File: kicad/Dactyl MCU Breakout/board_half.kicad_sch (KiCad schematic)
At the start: 18 parts, among them J3 Columns, J4 Thumbs, J5 Rows, J6 Extrernal, J7 Split, J8 JST, SW1 LED, SW2 Reset, SW3 Battery, U1 Nice!Nano/2040

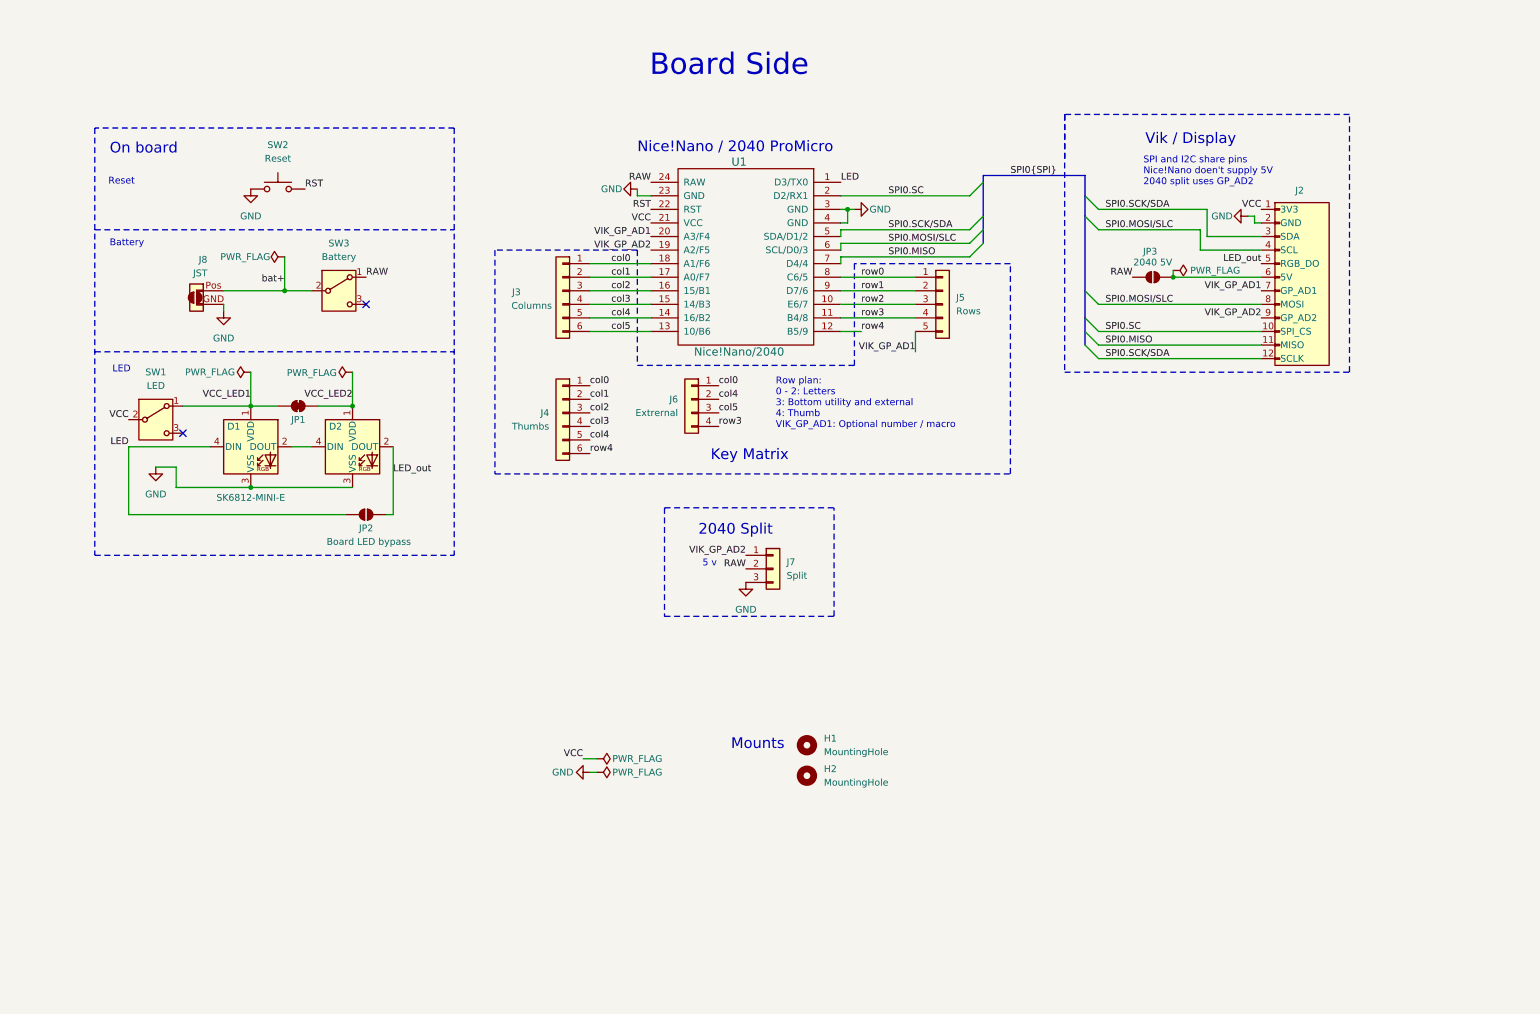
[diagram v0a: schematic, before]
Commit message: feat: add column to thumb, shift split to Vik AD1
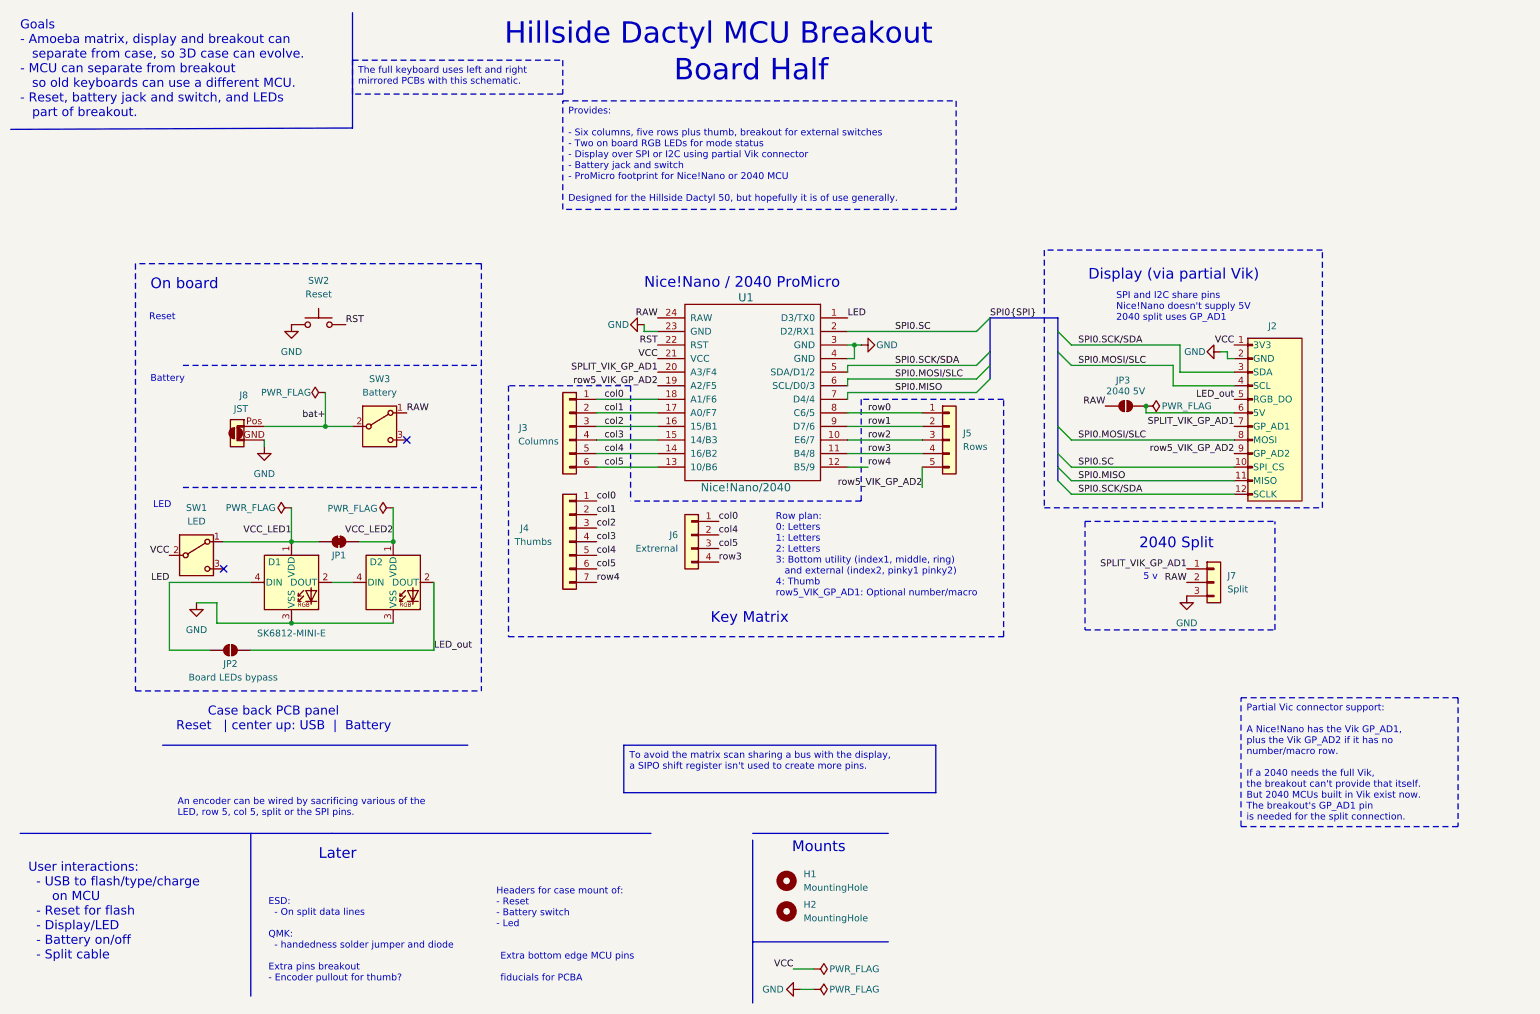
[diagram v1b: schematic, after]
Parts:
- removed J4: Thumbs, Connector_PinHeader_2.54mm:PinHeader_1x06_P2.54mm_Vertical, symbol Connector_Generic:Conn_01x06
- added J4: Thumbs, symbol Connector_Generic:Conn_01x07
- JP2: value Board LED bypass -> Board LEDs bypass
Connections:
- net col0: now also J4.1 (Pin_1)
- net col1: now also J4.2 (Pin_2)
- net col2: now also J4.3 (Pin_3)
- net col3: now also J4.4 (Pin_4)
- net col4: now also J4.5 (Pin_5)
- net col5: now also J4.6 (Pin_6)
- net row4: now also J4.7 (Pin_7)
- net VIK_GP_AD1 renamed SPLIT_VIK_GP_AD1
- net SPLIT_VIK_GP_AD1: now also J7.1 (Pin_1); no longer J5.5 (Pin_5)
- net VIK_GP_AD2 renamed row5_VIK_GP_AD2
- net row5_VIK_GP_AD2: now also J5.5 (Pin_5); no longer J7.1 (Pin_1)
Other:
- note added: "${TITLE}"
- note added: "An encoder can be wired by sacrificing various of the LED, row 5, col 5, split or the SPI pins."
- note added: "Board Half"
- note added: "Case back PCB panel Reset | center up: USB | Battery"
- note added: "Display (via partial Vik)"
- note added: "ESD: - On split data lines QMK: - handedness solder jumper and diode Extra pins breakout - Encoder pullout for thumb?"
- note added: "Extra bottom edge MCU pins fiducials for PCBA"
- note added: "Goals - Amoeba matrix, display and breakout can separate from case, so 3D case can evolve. - MCU can separate from breakout so old keyboards can use a different MCU. - Reset, battery jack and switch, and LEDs part of breakout."
- note added: "Headers for case mount of: - Reset - Battery switch - Led"
- note added: "Later"
- note added: "Row plan: 0: Letters 1: Letters 2: Letters 3: Bottom utility (index1, middle, ring) and external (index2, pinky1 pinky2) 4: Thumb row5_VIK_GP_AD1: Optional number/macro"
- note added: "SPI and I2C share pins Nice!Nano doesn't supply 5V 2040 split uses GP_AD1"
- note added: "User interactions: - USB to flash/type/charge on MCU - Reset for flash - Display/LED - Battery on/off - Split cable"
- note removed: "Board Side"
- note removed: "Row plan: 0 - 2: Letters 3: Bottom utility and external 4: Thumb VIK_GP_AD1: Optional number / macro"
- note removed: "SPI and I2C share pins Nice!Nano doen't supply 5V 2040 split uses GP_AD2"
- note removed: "Vik / Display"
- title: (none) -> Hillside Dactyl MCU Breakout
- moved on the sheet: D1, D2, H1, H2, J2, J3, J5, J6, J7, J8, JP1, JP2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

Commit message: feat: finish wiring
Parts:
- removed JP3: 2040 5V, Jumper:SolderJumper-2_P1.3mm_Bridged_RoundedPad1.0x1.5mm, symbol Jumper:SolderJumper_2_Open
- added J5: Display, Connector_PinHeader_2.54mm:PinHeader_1x05_P2.54mm_Vertical, symbol Connector_Generic:Conn_01x05
- added JP3: SCK term, Jumper:SolderJumper-2_P1.3mm_Bridged_RoundedPad1.0x1.5mm, symbol Jumper:SolderJumper_2_Bridged
- D1, D2: footprint Dactyl:SK6812-MINI-E-Dog2 -> Dactyl:SK6812-MINI-E-Dog2_1S
- H1, H2: footprint MountingHole:MountingHole_3.2mm_M3_DIN965_Pad -> MountingHole:MountingHole_3.2mm_M3_DIN965
- J3: renamed from J4; footprint (none) -> Connector_PinHeader_2.54mm:PinHeader_1x07_P2.54mm_Vertical
- J6: value Extrernal -> External
- J9: renamed from J2; value ~ -> Vic; footprint (none) -> Dactyl:vik-keyboard-connector-horizontal; LCSC Part # (none) -> C2906115
- JP2: value Board LEDs bypass -> LEDs bypass
- SW1: renamed from SW3; LCSC Part # (none) -> C221662
- SW4: renamed from SW1; LCSC Part # (none) -> C221662
- U1: footprint Dactyl:ProMicro_unrouted -> Dactyl:ProMicro_v2_1
- renumbered J3 to J1, J5 to J2, J8 to J7, J7 to J8
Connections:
- net GND: now also J7.1 (GND), J5.4 (Pin_4); no longer J7.GND
- net LED: now also U1.10 (E6/7); no longer U1.1 (D3/TX0)
- net RAW: now also J9.6 (5V)
- net SPI0.SC: now also J5.5 (Pin_5)
- net SPI0.SCK/SDA: now also J5.2 (Pin_2), JP3.2 (B); no longer U1.5 (SDA/D1/2)
- net VCC: now also J5.3 (Pin_3)
- net bat+: now also J7.2 (Pos); no longer J7.Pos
- net row0: now also U1.1 (D3/TX0); no longer U1.8 (C6/5)
- net row1: now also U1.8 (C6/5); no longer U1.9 (D7/6)
- net row2: now also U1.9 (D7/6); no longer U1.10 (E6/7)
- net SPI0.MISO renamed SPI0.CIPO
- net SPI0.MOSI/SLC renamed SPI0.COPI/SCL
- net SPI0.COPI/SCL: now also J5.1 (Pin_1)
- new net: JP3.1 (A), U1.5 (SDA/D1/2)
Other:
- note added: "Display and partial Vik"
- note added: "ESD: - On split data lines QMK: - handedness solder jumper and diode Extra pins breakout - Encoder pullout for thumb? Jumper on ViK 5v to cut off Nice!Nano 3.3v?"
- note removed: "Display (via partial Vik)"
- note removed: "ESD: - On split data lines QMK: - handedness solder jumper and diode Extra pins breakout - Encoder pullout for thumb?"
- moved on the sheet: J1, J2, J3, J6, J8, J9, U1

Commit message: feat: area reserved for TRRS. base plate notch
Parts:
- JP2: value LEDs bypass -> Vik LED bypass; footprint Jumper:SolderJumper-2_P1.3mm_Bridged_RoundedPad1.0x1.5mm -> Jumper:SolderJumper-2_P1.3mm_Open_RoundedPad1.0x1.5mm
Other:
- moved on the sheet: J2, J8
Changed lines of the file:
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@@
 	(wire
 		(pts
-			(xy 173.99 93.98) (xy 168.91 93.98)
+			(xy 176.53 93.98) (xy 168.91 93.98)
 		)
 		(stroke
@@
 		)
 	)
-	(wire
-		(pts
-			(xy 190.5 93.98) (xy 190.5 97.79)
-		)
-		(stroke
-			(width 0)
-			(type default)
-		)
-	)
 	(polyline
 		(pts
-			(xy 172.72 100.33) (xy 128.27 100.33)
+			(xy 173.99 100.33) (xy 128.27 100.33)
 		)
 		(stroke
@@
 	(polyline
 		(pts
-			(xy 172.72 81.28) (xy 172.72 100.33)
+			(xy 173.99 81.28) (xy 173.99 100.33)
 		)
 		(stroke
@@
 	(wire
 		(pts
-			(xy 168.91 91.44) (xy 190.5 91.44)
+			(xy 168.91 91.44) (xy 191.77 91.44)
 		)
 		(stroke
@@
 	(polyline
 		(pts
-			(xy 198.12 148.59) (xy 198.12 128.27)
+			(xy 171.45 148.59) (xy 171.45 128.27)
 		)
 		(stroke
@@
 	(polyline
 		(pts
-			(xy 204.47 81.28) (xy 172.72 81.28)
+			(xy 204.47 81.28) (xy 173.99 81.28)
 		)
 		(stroke
@@
 	(polyline
 		(pts
-			(xy 162.56 128.27) (xy 162.56 148.59)
+			(xy 135.89 128.27) (xy 135.89 148.59)
 		)
 		(stroke
@@
 	(wire
 		(pts
-			(xy 180.34 86.36) (xy 190.5 86.36)
+			(xy 180.34 86.36) (xy 191.77 86.36)
 		)
 		(stroke
@@
 	(wire
 		(pts
-			(xy 177.8 88.9) (xy 190.5 88.9)
+			(xy 177.8 88.9) (xy 191.77 88.9)
 		)
 		(stroke
@@
 	(polyline
 		(pts
-			(xy 97.79 149.86) (xy 40.64 149.86)
+			(xy 97.79 54.61) (xy 40.64 54.61)
 		)
 		(stroke
@@
 	(wire
 		(pts
+			(xy 191.77 93.98) (xy 191.77 97.79)
+		)
+		(stroke
+			(width 0)
+			(type default)
+		)
+	)
+	(wire
+		(pts
 			(xy 50.8 127) (xy 64.77 127)
 		)
@@
 	(wire
 		(pts
+			(xy 191.77 83.82) (xy 190.5 83.82)
+		)
+		(stroke
+			(width 0)
+			(type default)
+		)
+	)
+	(wire
+		(pts
 			(xy 251.46 76.2) (xy 252.73 76.2)
 		)
@@
 	(polyline
 		(pts
-			(xy 162.56 128.27) (xy 198.12 128.27)
+			(xy 135.89 128.27) (xy 171.45 128.27)
 		)
 		(stroke
@@
 	(polyline
 		(pts
-			(xy 162.56 148.59) (xy 198.12 148.59)
+			(xy 135.89 148.59) (xy 171.45 148.59)
 		)
 		(stroke
@@
 		)
 	)
-	(text_box "Partial Vic connector support:\n\nA Nice!Nano has the Vik GP_AD1, plus the Vik GP_AD2 if it has no number/macro row.\n\nIf a 2040 needs the full Vik, the breakout can't provide that itself.\nBut 2040 MCUs built in Vik exist now."
+	(text_box "Partial Vic connector support:\n\nA Nice!Nano has the Vik GP_AD1, plus the Vik GP_AD2 \nif it has no number/macro row.\n\nIf a 2040 needs the full Vik, the breakout can't provide it.\nBut 2040 MCUs with built in Vik now exist."
 		(exclude_from_sim no)
-		(at 213.36 149.86 0)
-		(size 69.85 15.24)
+		(at 219.71 127 0)
+		(size 60.96 15.24)
 		(stroke
 			(width 0)
@@
 	(text "        Case back PCB panel\nReset   | center up: USB  |  Battery\n"
 		(exclude_from_sim no)
-		(at 43.18 147.32 0)
+		(at 43.18 52.07 0)
 		(effects
 			(font
@@
 	(text "2040 Split"
 		(exclude_from_sim no)
-		(at 172.72 133.604 0)
+		(at 146.05 133.604 0)
 		(effects
 			(font
@@
 	(text "5 v \n"
 		(exclude_from_sim no)
-		(at 173.482 139.446 0)
+		(at 146.812 139.446 0)
 		(effects
 			(font
@@
 	)
 	(label "row5_VIK_GP_AD2"
-		(at 190.5 97.79 180)
+		(at 191.77 97.79 180)
 		(fields_autoplaced yes)
 		(effects
@@
 	)
 	(label "SPLIT_VIK_GP_AD1"
-		(at 181.61 137.16 180)
+		(at 154.94 137.16 180)
 		(fields_autoplaced yes)
 		(effects
@@
 	)
 	(label "row4"
-		(at 173.99 93.98 0)
+		(at 176.53 93.98 0)
 		(fields_autoplaced yes)
 		(effects
@@
 	)
 	(label "RAW"
-		(at 181.61 139.7 180)
+		(at 154.94 139.7 180)
 		(fields_autoplaced yes)
 		(effects
@@
 			)
 		)
-		(property "Value" "LEDs bypass"
+		(property "Value" "Vik LED bypass"
 			(at 53.848 137.16 0)
 			(effects
@@
 			)
 		)
-		(property "Footprint" "Jumper:SolderJumper-2_P1.3mm_Bridged_RoundedPad1.0x1.5mm"
+		(property "Footprint" "Jumper:SolderJumper-2_P1.3mm_Open_RoundedPad1.0x1.5mm"
 			(at 53.34 132.08 0)
 			(effects
@@
 	(symbol
 		(lib_id "Connector_Generic:Conn_01x05")
-		(at 195.58 88.9 0)
+		(at 196.85 88.9 0)
 		(unit 1)
 		(exclude_from_sim no)
@@
 		(dnp no)
 		(property "Reference" "J2"
-			(at 198.12 87.6299 0)
+			(at 199.39 87.6299 0)
 			(effects
 				(font
@@
 		)
 		(property "Value" "Rows"
-			(at 198.12 90.1699 0)
+			(at 199.39 90.1699 0)
 			(effects
 				(font
@@
 		)
 		(property "Footprint" "Connector_PinHeader_2.54mm:PinHeader_1x05_P2.54mm_Vertical"
-			(at 195.58 88.9 0)
+			(at 196.85 88.9 0)
 			(effects
 				(font
@@
 		)
 		(property "Datasheet" "~"
-			(at 195.58 88.9 0)
+			(at 196.85 88.9 0)
 			(effects
 				(font
@@
 		)
 		(property "Description" "Generic connector, single row, 01x05, script generated (kicad-library-utils/schlib/autogen/connector/)"
-			(at 195.58 88.9 0)
+			(at 196.85 88.9 0)
 			(effects
 				(font
@@
 	(symbol
 		(lib_id "Connector_Generic:Conn_01x03")
-		(at 186.69 139.7 0)
+		(at 160.02 139.7 0)
 		(unit 1)
 		(exclude_from_sim no)
@@
 		(fields_autoplaced yes)
 		(property "Reference" "J8"
-			(at 189.23 138.4299 0)
+			(at 162.56 138.4299 0)
 			(effects
 				(font
@@
 		)
 		(property "Value" "Split"
-			(at 189.23 140.9699 0)
+			(at 162.56 140.9699 0)
 			(effects
 				(font
@@
 		)
 		(property "Footprint" "Connector_PinHeader_2.54mm:PinHeader_1x03_P2.54mm_Vertical"
-			(at 186.69 139.7 0)
+			(at 160.02 139.7 0)
 			(effects
 				(font
@@
 		)
 		(property "Datasheet" "~"
-			(at 186.69 139.7 0)
+			(at 160.02 139.7 0)
 			(effects
 				(font
@@
 		)
 		(property "Description" ""
-			(at 186.69 139.7 0)
+			(at 160.02 139.7 0)
 			(effects
 				(font
@@
 	(symbol
 		(lib_id "power:GND")
-		(at 181.61 142.24 0)
+		(at 154.94 142.24 0)
 		(unit 1)
 		(exclude_from_sim no)
@@
 		(fields_autoplaced yes)
 		(property "Reference" "#PWR04"
-			(at 181.61 148.59 0)
+			(at 154.94 148.59 0)
 			(effects
 				(font
@@
 		)
 		(property "Value" "GND"
-			(at 181.61 147.32 0)
+			(at 154.94 147.32 0)
 			(effects
 				(font
@@
 		)
 		(property "Footprint" ""
-			(at 181.61 142.24 0)
+			(at 154.94 142.24 0)
 			(effects
 				(font
@@
 		)
 		(property "Datasheet" ""
-			(at 181.61 142.24 0)
+			(at 154.94 142.24 0)
 			(effects
 				(font
@@
 		)
 		(property "Description" "Power symbol creates a global label with name \"GND\" , ground"
-			(at 181.61 142.24 0)
+			(at 154.94 142.24 0)
 			(effects
 				(font

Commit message: feat: left: reset and batt, right: two inserts
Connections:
- net GND: now also SW2.1; no longer SW2.2
- net RAW: now also SW1.3 (C); no longer SW1.1 (A)
- net RST: now also SW2.2; no longer SW2.1
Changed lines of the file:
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@@
 	)
 	(no_connect
-		(at 86.36 92.71)
+		(at 86.36 87.63)
 	)
 	(bus_entry
@@
 	)
 	(label "RAW"
-		(at 86.36 87.63 0)
+		(at 86.36 92.71 0)
 		(fields_autoplaced yes)
 		(effects
@@
 	)
 	(label "RST"
-		(at 74.93 71.12 0)
+		(at 64.77 71.12 180)
 		(fields_autoplaced yes)
 		(effects
@@
 				(size 1.27 1.27)
 			)
-			(justify left bottom)
+			(justify right bottom)
 		)
 	)
@@
 	(symbol
 		(lib_id "power:GND")
-		(at 64.77 71.12 0)
+		(at 74.93 71.12 0)
 		(mirror y)
 		(unit 1)
@@
 		(fields_autoplaced yes)
 		(property "Reference" "#PWR010"
-			(at 64.77 77.47 0)
+			(at 74.93 77.47 0)
 			(effects
 				(font
@@
 		)
 		(property "Value" "GND"
-			(at 64.77 76.2 0)
+			(at 74.93 76.2 0)
 			(effects
 				(font
@@
 		)
 		(property "Footprint" ""
-			(at 64.77 71.12 0)
+			(at 74.93 71.12 0)
 			(effects
 				(font
@@
 		)
 		(property "Datasheet" ""
-			(at 64.77 71.12 0)
+			(at 74.93 71.12 0)
 			(effects
 				(font
@@
 		)
 		(property "Description" "Power symbol creates a global label with name \"GND\" , ground"
-			(at 64.77 71.12 0)
+			(at 74.93 71.12 0)
 			(effects
 				(font
